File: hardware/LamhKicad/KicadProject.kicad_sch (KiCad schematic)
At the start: 26 parts, among them J1 Conn_ARM_JTAG_SWD_10, U1 TLV70433DBVT, U2 PCA9745BTW, U3 INA180A3, U5 TJA1051T-3, U6 STM32F072C8Tx

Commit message: Schematic update
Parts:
- removed D1: D_Schottky, symbol Device:D_Schottky
- removed R3: 10kΩ, symbol Device:R
- added C2: 100nF, symbol Device:C
- added C5: 100uF, symbol Device:C
- added J2: ESQ-110-X-X-D, SAMTEC_ESQ-110-14-G-D, symbol ESQ-110-X-X-D:ESQ-110-X-X-D
- added J3: 2060-1452/998-404, footprints:WAG, symbol Wago_2060-1452 998-404:2060-1452_998-404
- renumbered C14 to C1, C3 to C10, C4 to C11, C7 to C12, C6 to C13, C8 to C14, C9 to C15, C12 to C3, C13 to C4, C15 to C6, C5 to C7, C4 to C8, C3 to C9, R to R1, R to R2, R to R3, R2 to R4, R1 to R5, U5 to U1, U1 to U3, U3 to U4, U6 to U5
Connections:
- net +3.3V: now also C5.2
- net 5VLOGIC: now also J2.03, J2.04, J2.05, J2.06
- net CAN_hi: now also J2.16
- net CAN_lo: now also J2.15
- net GND: now also C2.2, C5.1, J2.01, J2.02, J2.07, J2.08, J2.14, J2.17, J2.18, J2.19, J2.20, J3.3 (2_1), J3.4 (2_2); no longer C1.1, C10.1, C11.1, C12.1, C13.1, C14.1, C15.1, C7.1, C8.1, C9.1, J1.1 (VTref), R1.1, R3.1, U1.5 (VIO), U2.28 (V_{DD}), U5.1 (VBAT), U5.24 (VDD), U5.36 (VDDIO2), U5.48 (VDD), U5.9 (VDDA)
- net CLK: now reaches U5.15 (PA5)
- net CLK: now also U2.26 (SCLK)
- net +5V renamed 5VSERVO
- net 5VSERVO: now also C2.1, J2.09, J2.10, J2.11, J2.12
- new net 3.3V: C1.1, C10.1, C11.1, C12.1, C13.1, C14.1, C15.1, C7.1, C8.1, C9.1, J1.1 (VTref), R1.1, R3.1, U1.5 (VIO), U2.28 (V_{DD}), U5.1 (VBAT), U5.24 (VDD), U5.36 (VDDIO2), U5.48 (VDD), U5.9 (VDDA)
- new net VBAT: J3.1 (1_1), J3.2 (1_2)
- no-connect marks 2 -> 4
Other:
- note added: "Connectors"
- note added: "Wago for main battery connection"
- note added: "interboard connector"
- note removed: "Unsure what connects"
- moved on the sheet: U4

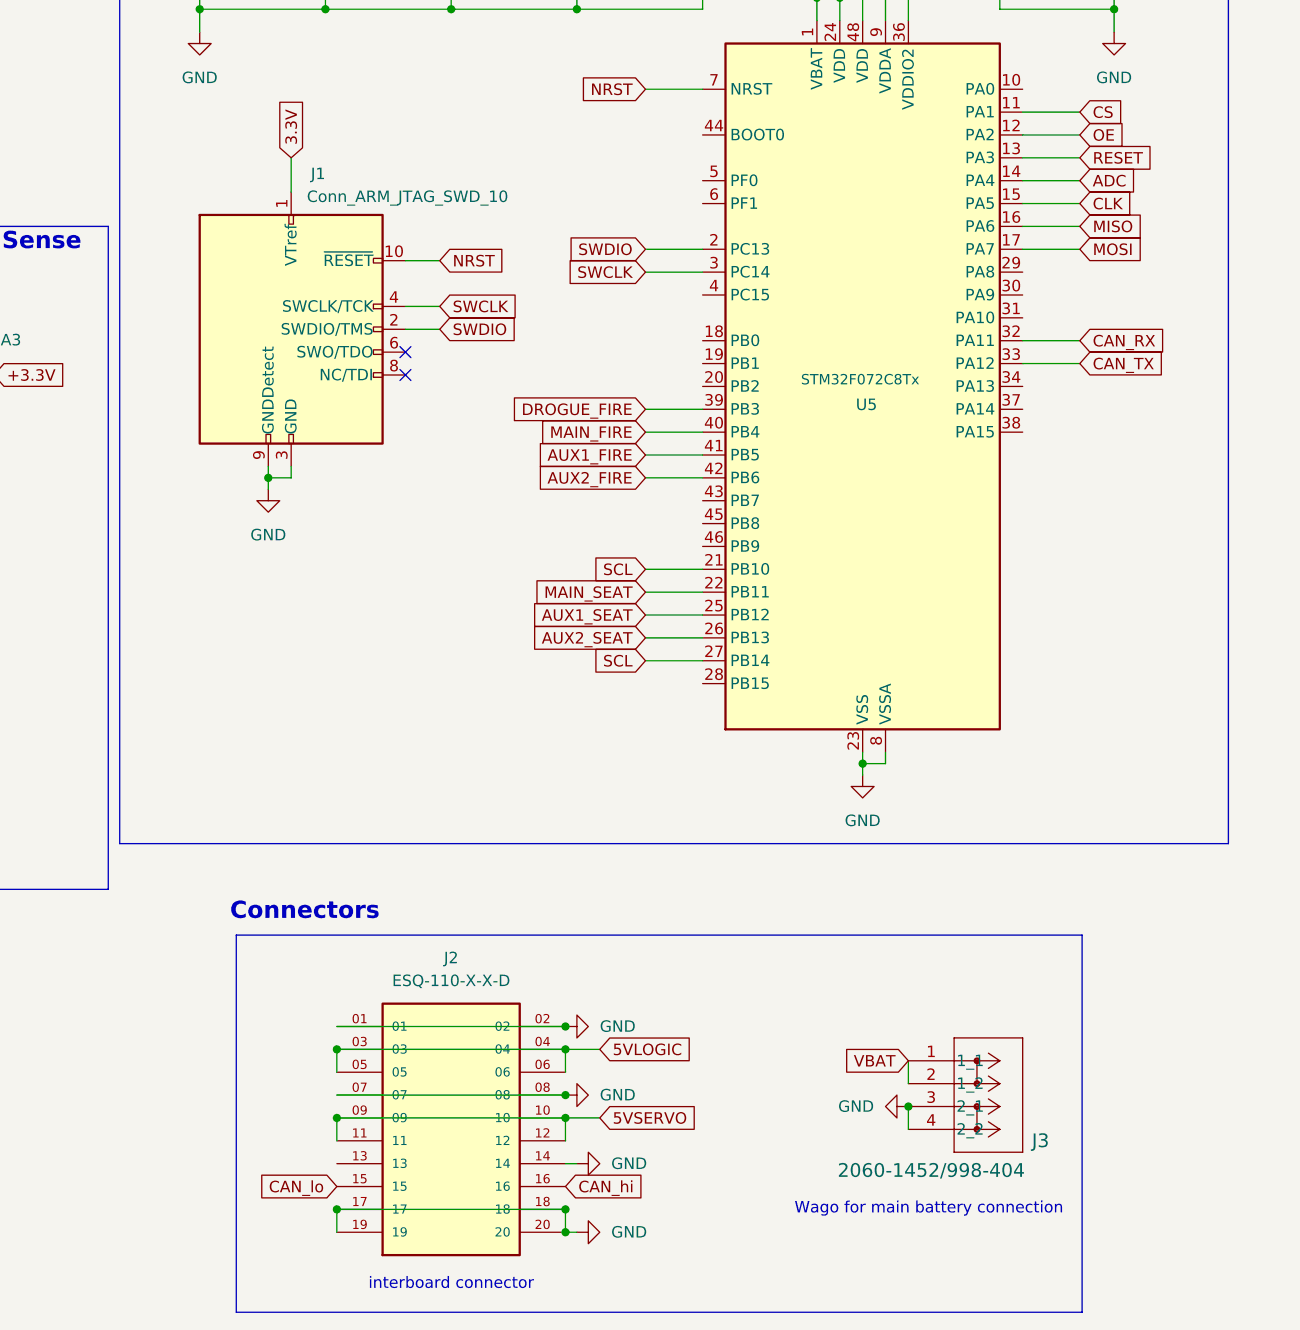
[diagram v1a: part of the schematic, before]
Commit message: Some fixes to PCB editor conversion
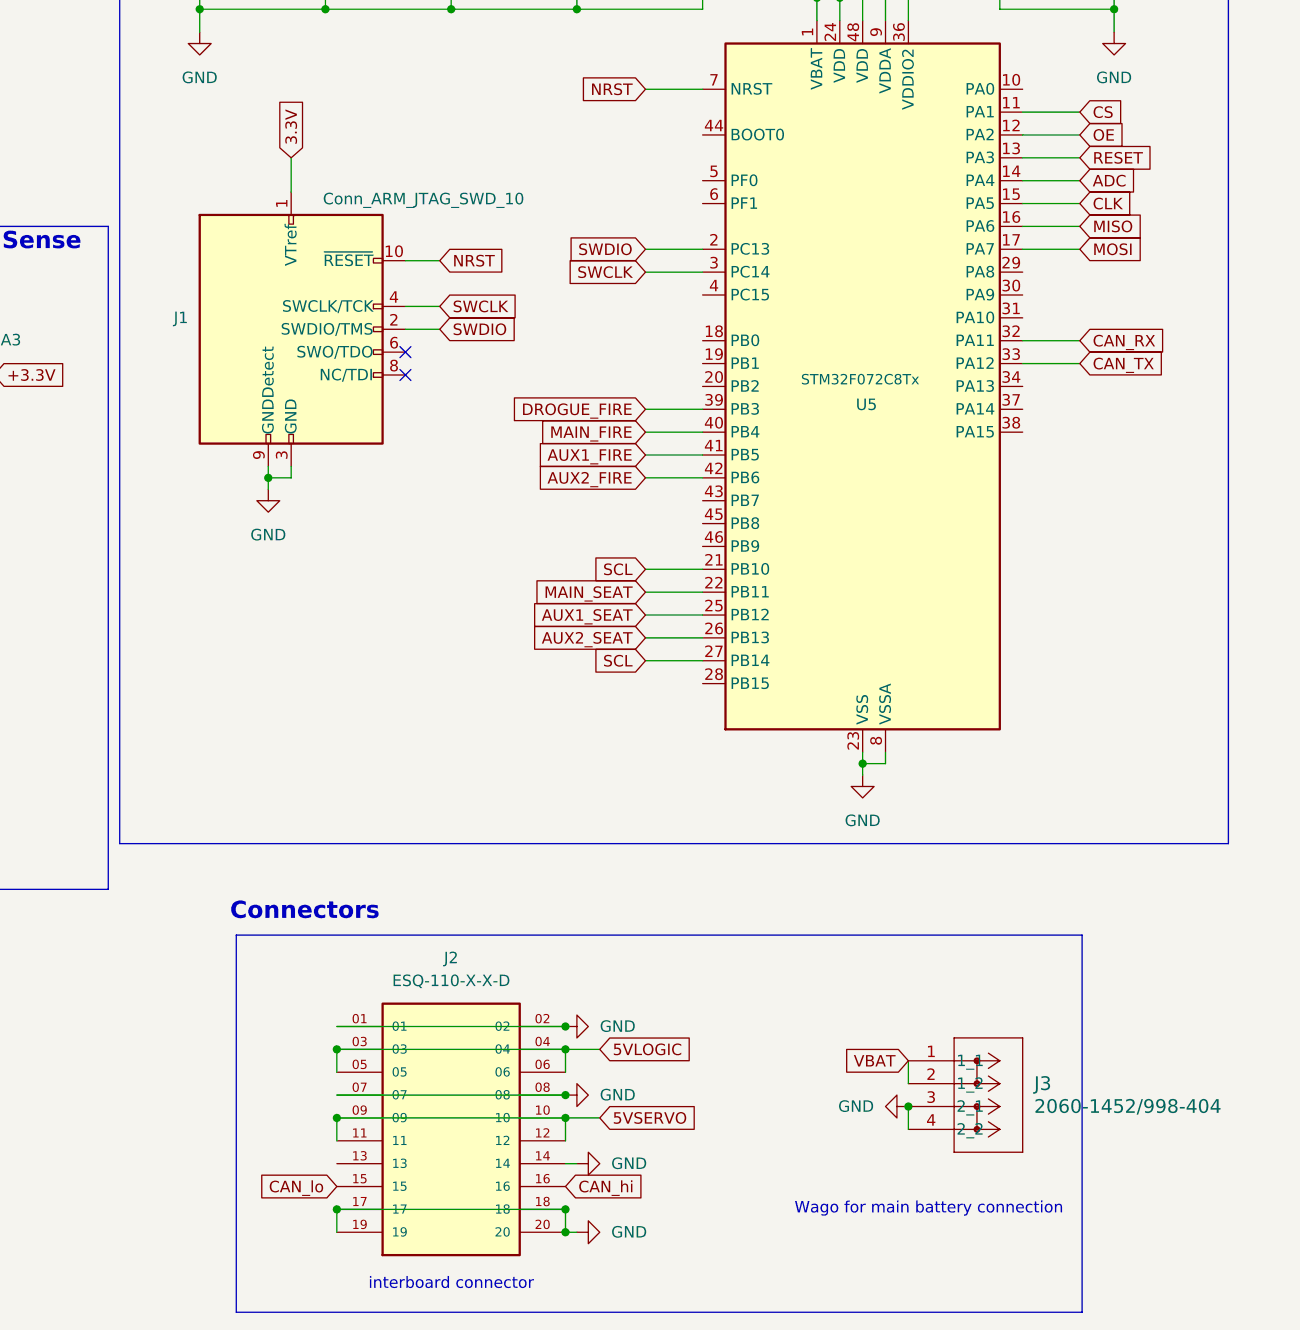
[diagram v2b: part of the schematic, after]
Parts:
- removed U3: TLV70433DBVT, DBV0005A_N, symbol 2026-01-14_10-49-14:TLV70433DBVT
- added U3: TLV70433DBVT, DBV0005A_N, symbol TLV70433DBVT:TLV70433DBVT
- J3: footprint footprints:WAG -> WAG
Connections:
- net +3.3V: now also U3.3 (OUT)
- net 5VSERVO: now also U3.2 (IN)
- net GND: now also U3.1 (GND)

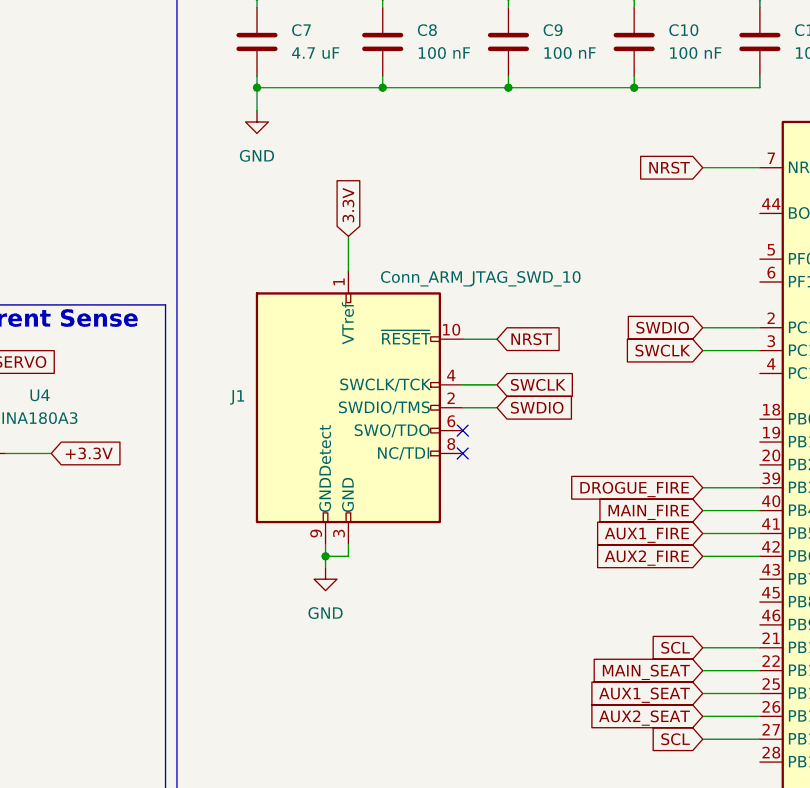
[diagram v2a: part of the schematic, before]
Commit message: Fixed all footprints
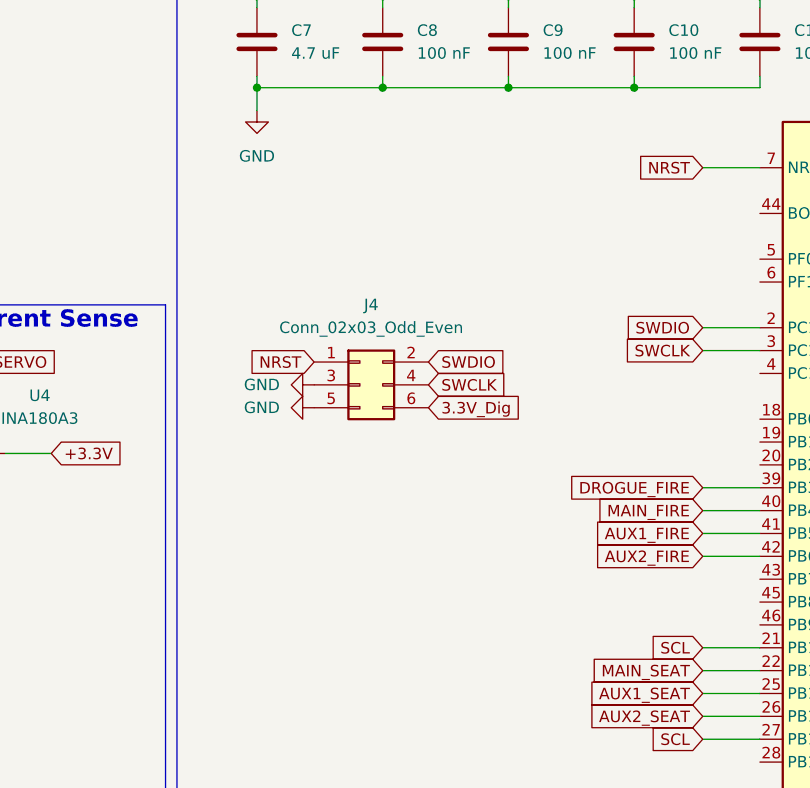
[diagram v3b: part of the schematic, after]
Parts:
- removed J1: Conn_ARM_JTAG_SWD_10, symbol Connector:Conn_ARM_JTAG_SWD_10
- added J4: Conn_02x03_Odd_Even, Connector_PinHeader_1.00mm:PinHeader_2x03_P1.00mm_Vertical, symbol Connector_Generic:Conn_02x03_Odd_Even
- C1, C10, C11, C12, C13, C14, C15, C2, C3, C4, C5, C6, C7, C8, C9, R1, R2, R3, R4, R5: footprint (none) -> Capacitor_SMD:C_0402_1005Metric
- J3: footprint WAG -> footprints:WAG
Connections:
- net GND: now also J4.3 (Pin_3), J4.5 (Pin_5)
- net NRST: now also J4.1 (Pin_1)
- net SWCLK: now also J4.4 (Pin_4)
- net SWDIO: now also J4.2 (Pin_2)
- new net 3.3V_Dig: J4.6 (Pin_6)
- no-connect marks 4 -> 2

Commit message: started
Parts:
- removed U4: INA180A3, Package_TO_SOT_SMD:SOT-23-5, symbol Amplifier_Current:INA180A3
- added J1: USB_C_Receptacle_USB2.0_16P, Connector_USB:USB_C_Receptacle_G-Switch_GT-USB-7010ASV, symbol Connector:USB_C_Receptacle_USB2.0_16P
- added J1: Conn_02x03_Odd_Even, Connector_PinHeader_1.00mm:PinHeader_2x03_P1.00mm_Vertical, symbol Connector_Generic:Conn_02x03_Odd_Even
- added R12, R13: 10K, Resistor_SMD:R_0402_1005Metric, symbol Device:R
- added R7, R8: 5.1K, Resistor_SMD:R_0402_1005Metric, symbol Device:R
- added U7: USBLC6-2SC6, Package_TO_SOT_SMD:SOT-23-6, symbol Power_Protection:USBLC6-2SC6
- R1, R2, R3, R4, R5: footprint Capacitor_SMD:C_0402_1005Metric -> Resistor_SMD:R_0402_1005Metric
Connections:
- net 5VLOGIC: now also C2.1, U3.2 (IN)
- net 5VSERVO: no longer C2.1, U3.2 (IN)
- net CAN_lo: now also J2.18; no longer J2.15
- net GND: now also J2.13, J2.15, J1.A1 (GND), J1.A12 (GND), J1.B1 (GND), J1.B12 (GND), J1.S1 (SHIELD), R13.1, R7.2, R8.1, U7.2 (GND); no longer J2.18
- net AUX1_FIRE: no longer names the net of U5.41 (PB5)
- net AUX2_FIRE: no longer names the net of U5.42 (PB6)
- net DROGUE_FIRE: no longer names the net of U5.39 (PB3)
- net MAIN_FIRE: no longer names the net of U5.40 (PB4)
- new net: J1.A7 (D-), J1.B7 (D-), U7.4 (I/O2)
- new net: J1.A6 (D+), J1.B6 (D+), U7.6 (I/O1)
- new net: J1.B5 (CC2), R8.2
- new net: J1.A5 (CC1), R7.1
- new net CAN_+: J1.2 (Pin_2)
- new net CAN_-: J1.1 (Pin_1)
- new net Mode_sel: R12.1, R13.2
- new net PA+: J1.4 (Pin_4)
- new net PA-: J1.3 (Pin_3)
- new net USB_D+: J1.6 (Pin_6), U7.1 (I/O1)
- new net USB_D-: J1.5 (Pin_5), U7.3 (I/O2)
- new net VBUS_RAW: J1.A4 (VBUS), J1.A9 (VBUS), J1.B4 (VBUS), J1.B9 (VBUS), R12.2, U7.5 (VBUS)
- no-connect marks 2 -> 4
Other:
- note added: "USB-C & mode select"
- note added: "rxd"
- note added: "txd"
- note removed: "Current Sense"
- moved on the sheet: C2, C5

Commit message: Changes
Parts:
- removed J1: USB_C_Receptacle_USB2.0_16P, Connector_USB:USB_C_Receptacle_G-Switch_GT-USB-7010ASV, symbol Connector:USB_C_Receptacle_USB2.0_16P
- removed J1: Conn_02x03_Odd_Even, Connector_PinHeader_1.00mm:PinHeader_2x03_P1.00mm_Vertical, symbol Connector_Generic:Conn_02x03_Odd_Even
- removed J3: 2060-1452/998-404, footprints:WAG, symbol Wago_2060-1452 998-404:2060-1452_998-404
- removed R1, R3: 10kΩ, Resistor_SMD:R_0402_1005Metric, symbol Device:R
- removed R12, R13: 10K, Resistor_SMD:R_0402_1005Metric, symbol Device:R
- removed R2: ISET, Resistor_SMD:R_0402_1005Metric, symbol Device:R
- removed R7, R8: 5.1K, Resistor_SMD:R_0402_1005Metric, symbol Device:R
- removed U2: PCA9745BTW, Package_SO:NXP_HTSSOP-28-1EP_4.4x9.7mm_P0.65mm_EP2.2x3.4mm, symbol Driver_LED:PCA9745BTW
- removed U7: USBLC6-2SC6, Package_TO_SOT_SMD:SOT-23-6, symbol Power_Protection:USBLC6-2SC6
- added D1: NUP2105L, Package_TO_SOT_SMD:SOT-23, symbol Power_Protection:NUP2105L
- added U2: PCA9685PW_112, TSSOP28_SOT361-1_NXP, symbol 2026-01-15_17-55-23:PCA9685PW_112
- renumbered J4 to J1, U5 to U4
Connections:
- net +3.3V is gone; now on net 3.3V: C5.2, U3.3 (OUT)
- net CAN_RX is gone; now on net CAN_-: U1.4 (RXD), U4.32 (PA11)
- net CAN_TX is gone; now on net CAN_+: U1.1 (TXD), U4.33 (PA12)
- net CAN_+: now also R4.1, U1.7 (CANH), D1.1 (K)
- net CAN_-: now also R5.2, U1.6 (CANL), D1.2 (K)
- net CAN_hi: no longer R4.1, U1.7 (CANH)
- net CAN_lo: no longer R5.2, U1.6 (CANL)
- net GND: now also D1.3 (A)
- no-connect marks 4 -> 2
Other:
- note removed: "USB-C & mode select"
- note removed: "rxd"
- note removed: "txd"

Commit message: cleaning up
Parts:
- removed J1: Conn_02x03_Odd_Even, Connector_PinHeader_1.00mm:PinHeader_2x03_P1.00mm_Vertical, symbol Connector_Generic:Conn_02x03_Odd_Even
- removed J2: ESQ-110-X-X-D, SAMTEC_ESQ-110-14-G-D, symbol ESQ-110-X-X-D:ESQ-110-X-X-D
- added J1: JTAG-10 PIN, Connector_IDC:IDC-Header_2x05_P2.54mm_Vertical, symbol Connector_Generic_MountingPin:Conn_01x10_MountingPin
- added J5: ESQ-110-X-X-D, SAMTEC_ESQ-110-14-G-D, symbol ESQ-110-X-X-D:ESQ-110-X-X-D
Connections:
- net 3.3V: now also J1.7 (Pin_7), J1.8 (Pin_8)
- net GND: now also J1.5 (Pin_5), J1.6 (Pin_6), J5.03, J5.04, J5.07, J5.08, J5.14, J5.19, J5.20
- net SWCLK: now also J1.2 (Pin_2), J5.17
- net SWDIO: now also J1.4 (Pin_4), J5.15
- net NRST renamed NRST4
- net NRST4: now also J1.1 (Pin_1), J5.12
- new net 5V_LOGIC: J5.05, J5.06
- new net 5v_SERVO: J5.01, J5.02
- new net CAN_o+: J5.16
- new net CAN_o-: J5.18
- no-connect marks 2 -> 10
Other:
- note added: "Decoupling Capacitors"
- note added: "Servo connectors"
- note removed: "Wago for main battery connection"
- moved on the sheet: C10, C11, C12, C13, C14, C15, C7, C8, C9, U2, U4

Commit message: updates, now just need the connector
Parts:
- added C16: 4700uf 16v, symbol Device:C_Polarized_US
- added C17: 10uF, Capacitor_SMD:C_0402_1005Metric, symbol Device:C
- added JP1, JP2, JP3, JP4: SolderJumper_2_Open, symbol Jumper:SolderJumper_2_Open
- added R1, R2, R3, R6: 220Ω, Resistor_SMD:R_0402_1005Metric, symbol Device:R
- added R10, R11, R12, R13, R9: 10kΩ, Resistor_SMD:R_0402_1005Metric, symbol Device:R
- added R7, R8: 4.7kΩ, Resistor_SMD:R_0402_1005Metric, symbol Device:R
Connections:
- net 3.3V: now also U2.28 (VDD), C17.2, JP1.1 (A), JP2.1 (A), JP3.1 (A), JP4.1 (A), R7.1, R8.1
- net 5v_SERVO: now also C16.1
- net GND: now also U2.14 (VSS), U2.25 (EXTCLK), C16.2, C17.1, R10.2, R11.1, R12.2, R13.2, R9.2
- net SCL: now also U2.26 (SCL), R7.2
- net at U2.1 (A0): now also JP1.2 (B), R9.1
- net at U2.2 (A1): now also JP2.2 (B), R10.1
- net at U2.23 (*OE): now also R11.2
- net SDA: now reaches U2.27 (SDA)
- net SDA: now also R8.2
- net at U2.3 (A2): now also JP3.2 (B), R12.1
- net at U2.4 (A3): now also JP4.2 (B), R13.1
- net at U2.6 (LED0): now also R1.2
- net at U2.7 (LED1): now also R2.2
- net at U2.8 (LED2): now also R3.2
- net at U2.9 (LED3): now also R6.2
- no-connect marks 10 -> 24
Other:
- note added: "3v3 LDO"
- note added: "Connector"
- note added: "Servos"
- note added: "XT60PW-M, our new battery connector for mach 2.5"
- note added: "decoupling cap"
- note added: "do we need reverse polarity protection?"
- note added: "lying on its side"
- note added: "to set address"
- note removed: "Connectors"
- note removed: "Decoupling Capacitors"
- note removed: "Local Logic"
- moved on the sheet: C1, C2, C3, C4, C5, C6, D1, R4, R5, U1, U2, U3

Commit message: progs, yes
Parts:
- added J2, J3, J4, J6: 436500303, MOLEX_436500303, symbol 436500303:436500303
- JP1, JP2, JP3, JP4: footprint (none) -> Jumper:SolderJumper-2_P1.3mm_Open_TrianglePad1.0x1.5mm
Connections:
- net 5VLOGIC: no longer C2.1, U3.2 (IN)
- net 5V_LOGIC: now also C2.1, U3.2 (IN)
- net 5v_SERVO: now also J2.3, J3.3, J4.3, J6.3
- net GND: now also J2.2, J2.S1 (SHIELD1), J2.S2 (SHIELD2), J3.2, J3.S1 (SHIELD1), J3.S2 (SHIELD2), J4.2, J4.S1 (SHIELD1), J4.S2 (SHIELD2), J6.2, J6.S1 (SHIELD1), J6.S2 (SHIELD2)
- net SCL: now also U4.45 (PB8); no longer U4.21 (PB10), U4.27 (PB14)
- net SDA: now also U4.43 (PB7)
- net at R3.1: now also J4.1
- net at R2.1: now also J3.1
- net at R1.1: now also J2.1
- net at R6.1: now also J6.1
- net AUX1_SEAT: no longer names the net of U4.25 (PB12)
- net AUX2_SEAT: no longer names the net of U4.26 (PB13)
- net MAIN_SEAT: no longer names the net of U4.22 (PB11)
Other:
- note removed: "Servo connectors"
